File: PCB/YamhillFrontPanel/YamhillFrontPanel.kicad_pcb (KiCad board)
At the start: 2 copper layers, 110 x 50 mm, 6 parts

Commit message: Rev A Front Panel
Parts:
- added C1: 100n, Capacitor_SMD:C_0805_2012Metric, F.Cu at (75.5, 113.0)
- added C10: 100n, Capacitor_SMD:C_0805_2012Metric, F.Cu at (110.0, 136.3)
- added C11: 100n, Capacitor_SMD:C_0805_2012Metric, F.Cu at (113.8, 136.3)
- added C12: 100n, Capacitor_SMD:C_0805_2012Metric, F.Cu at (101.3, 130.4)
- added C13: 100n, Capacitor_SMD:C_0805_2012Metric, F.Cu at (177.6, 101.8)
- added C14: 10n, Capacitor_SMD:C_0805_2012Metric, F.Cu at (106.6, 134.0)
- added C15: 100n, Capacitor_SMD:C_0805_2012Metric, F.Cu at (117.7, 138.6)
- added C16: 100n, Capacitor_SMD:C_0805_2012Metric, F.Cu at (164.7, 110.8)
- added C17: 100n, Capacitor_SMD:C_0805_2012Metric, F.Cu at (78.9, 54.3)
- added C18: 100n, Capacitor_SMD:C_0805_2012Metric, F.Cu at (117.7, 142.1)
- added C19: 100n, Capacitor_SMD:C_0805_2012Metric, F.Cu at (207.0, 65.0)
- added C2: 100n, Capacitor_SMD:C_0805_2012Metric, F.Cu at (71.9, 92.4)
- added C20: 100n, Capacitor_SMD:C_0805_2012Metric, F.Cu at (106.5, 142.1)
- added C21: 100n, Capacitor_SMD:C_0805_2012Metric, F.Cu at (207.0, 77.0)
- added C22: 100n, Capacitor_SMD:C_0805_2012Metric, F.Cu at (207.0, 89.0)
- added C23: 100n, Capacitor_SMD:C_0805_2012Metric, F.Cu at (207.0, 101.0)
- added C24: 10u, Capacitor_SMD:CP_Elec_4x4.5, F.Cu at (139.2, 85.9)
- added C25: 10n, Capacitor_SMD:C_0805_2012Metric, F.Cu at (146.6, 95.0)
- added C26: 1u, Capacitor_SMD:C_0805_2012Metric, F.Cu at (143.1, 136.0)
- added C27: 100n, Capacitor_SMD:C_0805_2012Metric, F.Cu at (158.2, 110.8)
- added C28: 1u, Capacitor_SMD:C_0805_2012Metric, F.Cu at (128.7, 99.3)
- added C29: 1u, Capacitor_SMD:C_0805_2012Metric, F.Cu at (146.6, 98.4)
- added C3: 100n, Capacitor_SMD:C_0805_2012Metric, F.Cu at (75.8, 80.0)
- added C30: 2.7n, Capacitor_SMD:C_0805_2012Metric, F.Cu at (146.6, 102.1)
- added C31: 10u, Capacitor_SMD:CP_Elec_4x4.5, F.Cu at (124.0, 107.2)
- added C32: 10u, Capacitor_SMD:CP_Elec_4x4.5, F.Cu at (111.9, 86.0)
- added C33: 10u, Capacitor_SMD:CP_Elec_4x4.5, F.Cu at (116.6, 64.4)
- added C34: 100n, Capacitor_SMD:C_0805_2012Metric, F.Cu at (100.5, 96.8)
- added C35: 1u, Capacitor_SMD:C_0805_2012Metric, F.Cu at (104.5, 96.8)
- added C36: 1u, Capacitor_SMD:C_0805_2012Metric, F.Cu at (124.4, 81.5)
- added C37: 1u, Capacitor_SMD:C_0805_2012Metric, F.Cu at (108.1, 68.8)
- added C38: 1u, Capacitor_SMD:C_0805_2012Metric, F.Cu at (85.2, 96.9)
- added C39: 100n, Capacitor_SMD:C_0805_2012Metric, F.Cu at (100.5, 101.4)
- added C4: 100n, Capacitor_SMD:C_0805_2012Metric, F.Cu at (71.9, 59.4)
- added C40: 100u, Capacitor_SMD:CP_Elec_6.3x5.9, F.Cu at (115.0, 108.2)
- added C41: 1u, Capacitor_SMD:C_0805_2012Metric, F.Cu at (111.3, 100.5)
- added C42: 1u, Capacitor_SMD:C_0805_2012Metric, F.Cu at (98.4, 74.5)
- added C43: 1u, Capacitor_SMD:C_0805_2012Metric, F.Cu at (129.4, 76.3)
- added C44: 100n, Capacitor_SMD:C_0805_2012Metric, F.Cu at (152.9, 107.0)
- added C45: 100n, Capacitor_SMD:C_0805_2012Metric, F.Cu at (157.5, 107.0)
- added C5: 100n, Capacitor_SMD:C_0805_2012Metric, F.Cu at (90.0, 126.1)
- added C6: 100n, Capacitor_SMD:C_0805_2012Metric, F.Cu at (90.0, 117.0)
- added C7: 100n, Capacitor_SMD:C_0805_2012Metric, F.Cu at (68.6, 113.0)
- added C8: 100n, Capacitor_SMD:C_0805_2012Metric, F.Cu at (68.6, 80.0)
- added C9: 100n, Capacitor_SMD:C_0805_2012Metric, F.Cu at (167.4, 141.5)
- added D1: MBRX120LF-TP, Diode_SMD:D_SOD-123, F.Cu at (200.0, 146.5)
- added D2: WS2812B, LED_SMD:LED_WS2812B_PLCC4_5.0x5.0mm_P3.2mm, B.Cu at (163.2, 118.7)
- added D3: WS2812B, LED_SMD:LED_WS2812B_PLCC4_5.0x5.0mm_P3.2mm, B.Cu at (72.0, 55.0)
- added D4: LED, LED_SMD:LED_0805_2012Metric, B.Cu at (203.0, 65.0)
- added D5: LED, LED_SMD:LED_0805_2012Metric, B.Cu at (203.0, 77.0)
- added D6: LED, LED_SMD:LED_0805_2012Metric, B.Cu at (203.0, 89.0)
- added D7: LED, LED_SMD:LED_0805_2012Metric, B.Cu at (203.0, 101.0)
- added J1: +3.3V In, Connector_PinHeader_2.54mm:PinHeader_1x02_P2.54mm_Vertical, F.Cu at (182.0, 147.0)
- added J10: Ext. ADC, Connector_PinHeader_2.54mm:PinHeader_1x08_P2.54mm_Vertical, F.Cu at (154.6, 147.0)
- added J11: CLK2, EtherkitKicadLibrary:SMA_Jack_Vertical, F.Cu at (68.0, 136.0)
- added J12: Mute, Connector_PinHeader_2.54mm:PinHeader_1x08_P2.54mm_Vertical, F.Cu at (128.0, 147.0)
- added J13: CLK4, EtherkitKicadLibrary:SMA_Jack_Vertical, F.Cu at (81.0, 136.0)
- added J14: REF_IN, EtherkitKicadLibrary:SMA_Jack_Vertical, F.Cu at (94.0, 136.0)
- added J15: Mic Power Jumper, Connector_PinHeader_2.54mm:PinHeader_1x02_P2.54mm_Vertical, F.Cu at (138.0, 109.8)
- added J16: Microphone, Connector_RJ:RJ45_OST_PJ012-8P8CX_Vertical, B.Cu at (155.0, 120.0)
- added J17: Mic Output, Connector_PinHeader_2.54mm:PinHeader_1x02_P2.54mm_Vertical, F.Cu at (150.4, 137.9)
- added J18: AF In, Connector_PinHeader_2.54mm:PinHeader_1x02_P2.54mm_Vertical, F.Cu at (84.3, 104.2)
- added J19: AF Jumper, Connector_PinHeader_2.54mm:PinHeader_1x02_P2.54mm_Vertical, F.Cu at (123.4, 86.3)
- added J2: Paddles, EtherkitKicadLibrary:Kycon_STX-3680-5NB, B.Cu at (97.0, 122.0)
- added J20: Speaker, EtherkitKicadLibrary:Ole_Wolff_OWS-091630W50A-8, F.Cu at (70.0, 124.0)
- added J21: Headphones, EtherkitKicadLibrary:Kycon_STX-3680-5NB, B.Cu at (110.0, 122.0)
- added J22: I/Q In, Connector_PinHeader_2.54mm:PinHeader_1x03_P2.54mm_Vertical, F.Cu at (152.5, 102.7)
- added J3: +5V In, Connector_PinHeader_2.54mm:PinHeader_1x02_P2.54mm_Vertical, F.Cu at (192.0, 147.0)
- added J4: USB VBUS, Connector_PinHeader_2.54mm:PinHeader_1x02_P2.54mm_Vertical, F.Cu at (205.0, 147.0)
- added J5: UART, Connector_PinHeader_2.54mm:PinHeader_1x03_P2.54mm_Vertical, F.Cu at (217.2, 109.9)
- added J6: Transmit, Connector_PinHeader_2.54mm:PinHeader_1x10_P2.54mm_Vertical, F.Cu at (95.0, 147.0)
- added J7: GPIO, Connector_PinHeader_2.54mm:PinHeader_1x12_P2.54mm_Vertical, F.Cu at (154.2, 91.9)
- added J8: CLK0, EtherkitKicadLibrary:SMA_Jack_Vertical, F.Cu at (55.0, 136.0)
- added J9: Osc Outputs, Connector_PinHeader_2.54mm:PinHeader_1x04_P2.54mm_Vertical, F.Cu at (78.5, 147.0)
- added L1: Fair-Rite 2512066017Y1, Inductor_SMD:L_1206_3216Metric, F.Cu at (146.2, 140.1)
- added Q1: 2N7002, Package_TO_SOT_SMD:SOT-23, F.Cu at (124.5, 75.5)
- added Q2: 2N7002, Package_TO_SOT_SMD:SOT-23, F.Cu at (103.4, 73.8)
- added Q3: 2N7002, Package_TO_SOT_SMD:SOT-23, F.Cu at (123.2, 134.4)
- added Q4: 2N7002, Package_TO_SOT_SMD:SOT-23, F.Cu at (118.2, 125.6)
- added R1: 47k, Resistor_SMD:R_0805_2012Metric, F.Cu at (161.0, 130.0)
- added R10: 47, Resistor_SMD:R_0805_2012Metric, F.Cu at (121.8, 138.6)
- added R11: 47, Resistor_SMD:R_0805_2012Metric, F.Cu at (121.8, 142.1)
- added R12: 10k, Resistor_SMD:R_0805_2012Metric, F.Cu at (177.6, 98.4)
- added R13: 10k, Resistor_SMD:R_0805_2012Metric, F.Cu at (102.6, 142.1)
- added R14: 10k, Resistor_SMD:R_0805_2012Metric, F.Cu at (177.6, 105.3)
- added R15: 470, Resistor_SMD:R_0805_2012Metric, F.Cu at (176.5, 143.4)
- added R16: 47, Resistor_SMD:R_0805_2012Metric, F.Cu at (106.5, 138.5)
- added R17: 4.7k, Resistor_SMD:R_0805_2012Metric, F.Cu at (127.6, 136.9)
- added R18: 4.7k, Resistor_SMD:R_0805_2012Metric, F.Cu at (127.5, 140.3)
- added R19: 330, Resistor_SMD:R_0805_2012Metric, F.Cu at (203.0, 65.0)
- added R2: 47k, Resistor_SMD:R_0805_2012Metric, F.Cu at (161.0, 125.0)
- added R20: 330, Resistor_SMD:R_0805_2012Metric, F.Cu at (203.0, 77.0)
- added R21: 330, Resistor_SMD:R_0805_2012Metric, F.Cu at (203.0, 89.0)
- added R22: 330, Resistor_SMD:R_0805_2012Metric, F.Cu at (203.0, 101.0)
- added R23: 7.5k, Resistor_SMD:R_0805_2012Metric, F.Cu at (131.3, 109.8)
- added R24: 47, Resistor_SMD:R_0805_2012Metric, F.Cu at (145.3, 90.3)
- added R25: 470, Resistor_SMD:R_0805_2012Metric, F.Cu at (136.0, 104.7)
- added R26: 5k trim, EtherkitKicadLibrary:Bournes_PTV09A, F.Cu at (136.0, 132.0)
- added R27: 10k, Resistor_SMD:R_0805_2012Metric, F.Cu at (133.3, 88.2)
- added R28: 10k, Resistor_SMD:R_0805_2012Metric, F.Cu at (140.8, 102.1)
- added R29: 100k, Resistor_SMD:R_0805_2012Metric, F.Cu at (132.4, 99.3)
- added R3: 47k, Resistor_SMD:R_0805_2012Metric, F.Cu at (161.0, 135.0)
- added R30: 10k, Resistor_SMD:R_0805_2012Metric, F.Cu at (128.7, 104.7)
- added R31: 470, Resistor_SMD:R_0805_2012Metric, F.Cu at (128.7, 93.6)
- added R32: 270k, Resistor_SMD:R_0805_2012Metric, F.Cu at (132.4, 93.6)
- added R33: 10k, Resistor_SMD:R_0805_2012Metric, F.Cu at (132.4, 104.7)
- added R34: 10k, Resistor_SMD:R_0805_2012Metric, F.Cu at (106.5, 86.1)
- added R35: 47, Resistor_SMD:R_0805_2012Metric, F.Cu at (117.5, 70.4)
- added R36: 100k, Resistor_SMD:R_0805_2012Metric, F.Cu at (107.8, 79.8)
- added R37: 100k, Resistor_SMD:R_0805_2012Metric, F.Cu at (120.4, 80.6)
- added R38: 10k, Resistor_SMD:R_0805_2012Metric, F.Cu at (117.2, 86.1)
- added R39: 47, Resistor_SMD:R_0805_2012Metric, F.Cu at (104.5, 92.8)
- added R4: 47, Resistor_SMD:R_0805_2012Metric, F.Cu at (109.9, 132.9)
- added R40: 1k, Resistor_SMD:R_0805_2012Metric, F.Cu at (112.0, 68.8)
- added R41: 100, Resistor_SMD:R_0805_2012Metric, F.Cu at (85.2, 92.0)
- added R42: 10k, EtherkitKicadLibrary:Alps_RK09L1140, B.Cu at (126.0, 122.0)
- added R43: 10k, Resistor_SMD:R_0805_2012Metric, F.Cu at (120.4, 75.5)
- added R44: 150, Resistor_SMD:R_0805_2012Metric, F.Cu at (117.9, 117.9)
- added R45: 100k, Resistor_SMD:R_0805_2012Metric, F.Cu at (104.9, 107.4)
- added R46: 1k, Resistor_SMD:R_0805_2012Metric, F.Cu at (107.8, 74.4)
- added R47: 100k, Resistor_SMD:R_0805_2012Metric, F.Cu at (100.5, 105.1)
- added R48: 470, Resistor_SMD:R_0805_2012Metric, F.Cu at (103.4, 68.8)
- added R49: 1k, Resistor_SMD:R_0805_2012Metric, F.Cu at (124.5, 70.0)
- added R5: 47, Resistor_SMD:R_0805_2012Metric, F.Cu at (113.8, 132.9)
- added R50: 100k, Resistor_SMD:R_0805_2012Metric, F.Cu at (98.4, 70.6)
- added R51: 100k, Resistor_SMD:R_0805_2012Metric, F.Cu at (129.4, 72.4)
- added R52: 4.7k, Resistor_SMD:R_0805_2012Metric, F.Cu at (118.2, 130.8)
- added R53: 4.7k, Resistor_SMD:R_0805_2012Metric, F.Cu at (118.2, 134.3)
- added R6: 47k, Resistor_SMD:R_0805_2012Metric, F.Cu at (164.0, 130.0)
- added R7: 47k, Resistor_SMD:R_0805_2012Metric, F.Cu at (164.0, 125.0)
- added R8: 47k, Resistor_SMD:R_0805_2012Metric, F.Cu at (164.0, 135.0)
- added R9: 47, Resistor_SMD:R_0805_2012Metric, F.Cu at (101.6, 138.7)
- added S1: PUSHBUTTON_TACTILE, EtherkitKicadLibrary:E-Switch_TL1105, B.Cu at (212.0, 65.0)
- added S2: PUSHBUTTON_TACTILE, EtherkitKicadLibrary:E-Switch_TL1105, B.Cu at (212.0, 77.0)
- added S3: PUSHBUTTON_TACTILE, EtherkitKicadLibrary:E-Switch_TL1105, B.Cu at (212.0, 89.0)
- added S4: PUSHBUTTON_TACTILE, EtherkitKicadLibrary:E-Switch_TL1105, B.Cu at (212.0, 101.0)
- added SW1: Tune, EtherkitKicadLibrary:Bournes_PEC11R-4xxxF-Sxxxx, B.Cu at (72.0, 101.0)
- added SW2: Multifunction, EtherkitKicadLibrary:Bournes_PEC11R-4xxxF-Sxxxx, B.Cu at (72.0, 68.0)
- added U1: 4" TFT LCD ST7796S, EtherkitKicadLibrary:ST7796_4.0in, B.Cu at (146.4, 83.0)
- added U2: ADS1115IDGS, Package_SO:TSSOP-10_3x3mm_P0.5mm, F.Cu at (162.2, 141.3)
- added U3: Pico, MCU_RaspberryPi_and_Boards:RPi_Pico_SMD_TH, F.Cu at (194.0, 126.7)
- added U4: ATX-H11-F-25.000MHZ-F25-T, EtherkitKicadLibrary:ASTX-H11-25.000MHZ-T, F.Cu at (101.4, 134.6)
- added U5: Si5351C, Package_DFN_QFN:VQFN-20-1EP_3x3mm_P0.45mm_EP1.55x1.55mm_ThermalVias, F.Cu at (112.0, 140.9)
- added U6: TCAL6416, Package_SO:TSSOP-24_6.1x7.8mm_P0.65mm, F.Cu at (188.1, 104.2)
- added U7: TLV9362, Package_SO:SOIC-8_3.9x4.9mm_P1.27mm, F.Cu at (139.3, 95.6)
- added U8: TLV9362, Package_SO:SOIC-8_3.9x4.9mm_P1.27mm, F.Cu at (114.1, 75.5)
- added U9: LM4875, Package_SO:TSSOP-8_3x3mm_P0.65mm, F.Cu at (106.0, 101.8)
- G***, Ref**: moved to F.Cu
- moved Ref** 119.5 mm to (90.1, 54.9), turned to 0 degrees
- moved G*** 105.7 mm to (206.0, 57.4), turned to 0 degrees
- moved H3 70.7 mm to (55.0, 145.0)
- moved H4 51.0 mm to (215.0, 145.0)
- moved H1 50.0 mm to (55.0, 55.0)
- moved H2 10.0 mm to (215.0, 55.0)
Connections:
- H1 pad 1: unconnected-(H1-Pad1) -> GNDD
- H2 pad 1: unconnected-(H2-Pad1) -> GNDD
- H3 pad 1: unconnected-(H3-Pad1) -> GNDD
- H4 pad 1: unconnected-(H4-Pad1) -> GNDD
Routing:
- net +5V: track 0.00 -> 431.4 mm, vias 0 -> 10
- net ENC1_A: track 0.00 -> 295.7 mm
- net ENC1_B: track 0.00 -> 289.8 mm, vias 0 -> 1
- net +3.3V: track 0.00 -> 284.7 mm, vias 0 -> 12
- net ENC2_B: track 0.00 -> 241.1 mm, vias 0 -> 2
- net ENC2_A: track 0.00 -> 237.8 mm, vias 0 -> 2
- net MUTE: track 0.00 -> 195.0 mm, vias 0 -> 5
- net ENC1_SW: track 0.00 -> 189.1 mm, vias 0 -> 1
- net SDA_3V3: track 0.00 -> 167.0 mm, vias 0 -> 3
- net SCL_3V3: track 0.00 -> 162.5 mm, vias 0 -> 3
- net ENC2_SW: track 0.00 -> 158.1 mm, vias 0 -> 2
- net Net-(D2-DOUT): track 0.00 -> 156.8 mm, vias 0 -> 2
- net SPI_TX: track 0.00 -> 149.7 mm
- net MCU_DAC: track 0.00 -> 141.5 mm, vias 0 -> 6
- net PDL_B: track 0.00 -> 134.0 mm, vias 0 -> 1
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- added copper zone on F.Cu, net GND
- added copper zone on B.Cu, net GNDD
- added copper zone on F.Cu, net GNDD
- removed copper zone on B.Cu, net (none)
- removed copper zone on F.Cu, net (none)
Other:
- board size 110 x 50 mm -> 170 x 100 mm
- board text added: "+3.3V"
- board text added: "+5V"
- board text added: "AF"
- board text added: "AIN0"
- board text added: "AIN1"
- board text added: "AIN2"
- board text added: "AIN3"
- board text added: "CLK0"
- board text added: "CLK1"
- board text added: "CLK2"
- board text added: "CLK3"
- board text added: "CLK4"
- board text added: "Front Panel Etherkit 2023"
- board text added: "GND"
- board text added: "I"
- board text added: "MIC GAIN"
- board text added: "Mic"
- board text added: "Mute"
- board text added: "P06"
- board text added: "P07"
- board text added: "P10"
- board text added: "P11"
- board text added: "P12"
- board text added: "P13"
- board text added: "Q"
- board text added: "REF IN"
- board text added: "RX"
- board text added: "TX"
- board text removed: "Sample Board Etherkit 2023"

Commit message: Update all PCBs for first tranche order
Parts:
- J20: footprint EtherkitKicadLibrary:Ole_Wolff_OWS-091630W50A-8 -> EtherkitKicadLibrary:CUI_CMS-160916-30-3; moved to B.Cu
- R26: footprint EtherkitKicadLibrary:Bournes_PTV09A -> EtherkitKicadLibrary:Bournes_PTV09A-4
- moved J20 2.57 mm to (72.5, 123.4), turned to 180 degrees
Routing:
- net +3.3V: track 284.7 -> 64.0 mm, vias 12 -> 10
- net GNDD: track 0.00 -> 91.0 mm, vias 4 -> 31
- net GND: track 0.00 -> 56.5 mm
- net Net-(J20-Pin_2): track 43.0 -> 59.4 mm, vias 0 -> 1
- net Net-(J20-Pin_1): track 48.7 -> 60.4 mm, vias 0 -> 1
- net Net-(C26-Pad2): track 11.7 -> 5.61 mm
- net PDL_A: track 126.1 -> 129.1 mm
- net Net-(U5-VDDOB): track 11.9 -> 14.7 mm
- net Net-(J14-In): track 23.0 -> 20.3 mm
- net +5V: track 431.4 -> 433.0 mm
- net PDL_B: track 134.0 -> 135.4 mm
- net Net-(D2-DOUT): track 156.8 -> 158.1 mm
- net CLK3: track 32.7 -> 33.9 mm
- net CLK2: track 52.5 -> 53.5 mm
- net MIC_SAMPLE: track 120.0 -> 119.0 mm
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- added copper zone on In2.Cu, net +3.3V
- added copper zone on In1.Cu, net GNDD
- removed copper zone on B.Cu, net GNDD
- removed copper zone on F.Cu, net GNDD
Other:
- copper layers 2 -> 4
- board text added: "Front Panel Etherkit 2024"
- board text removed: "Front Panel Etherkit 2023"

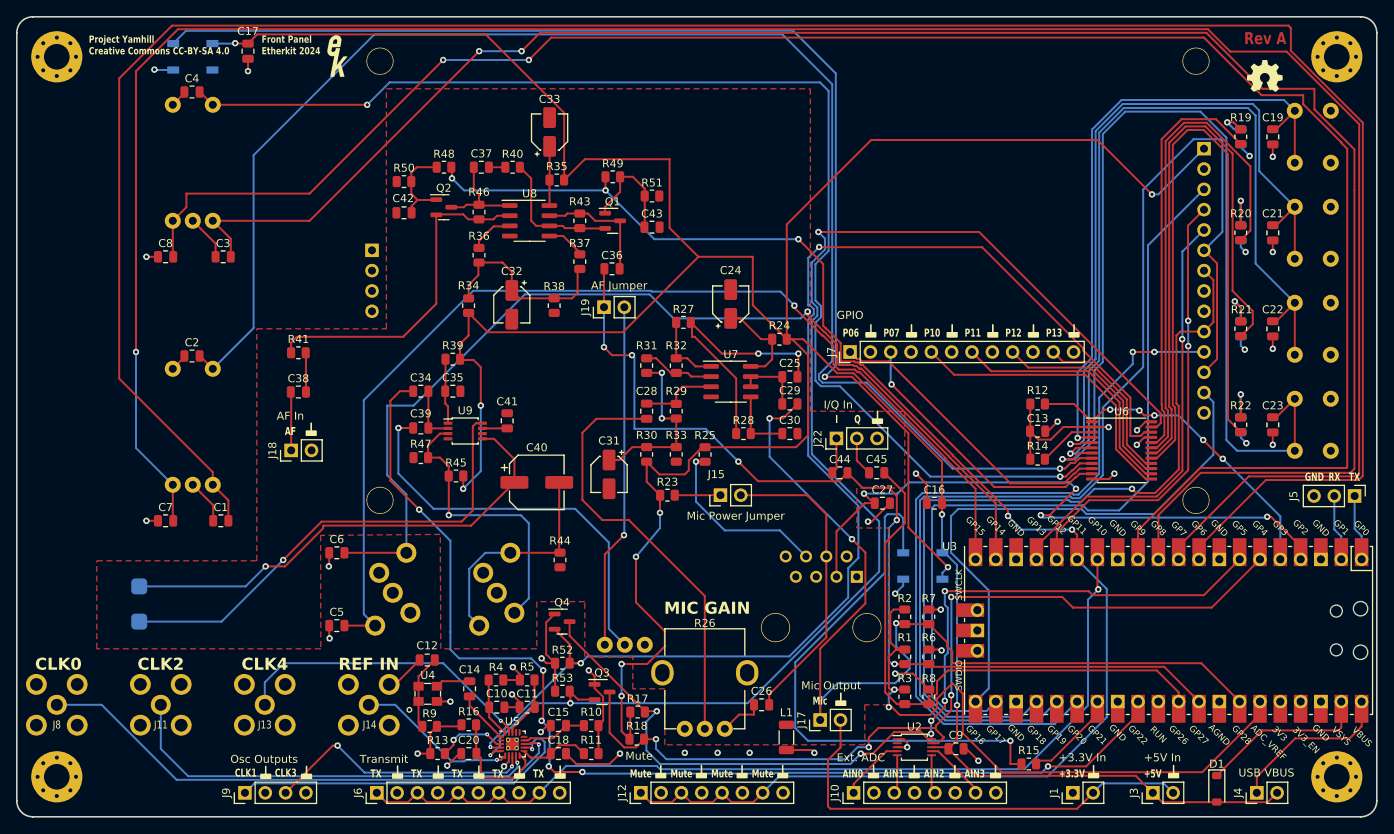
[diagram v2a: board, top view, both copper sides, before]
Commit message: Arch document update
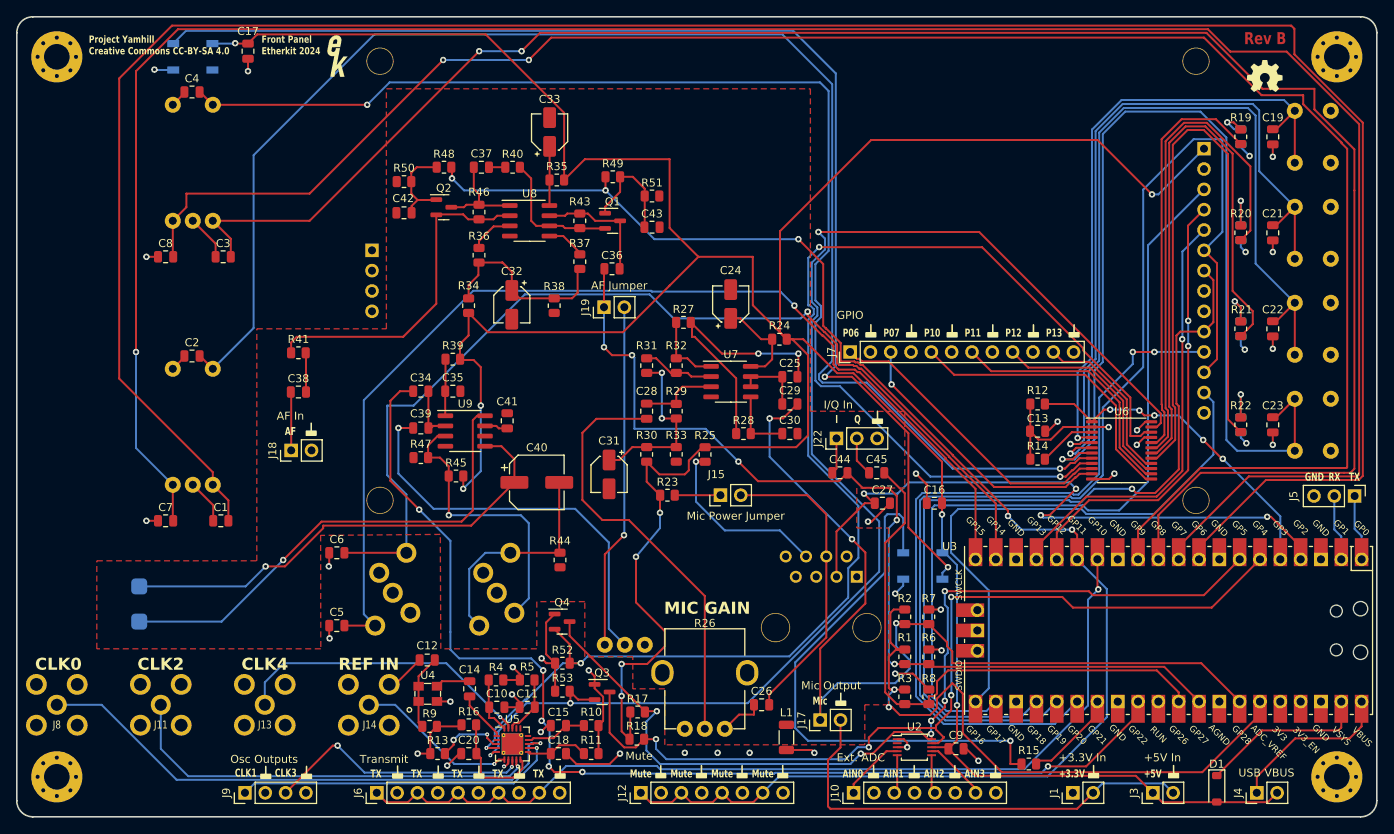
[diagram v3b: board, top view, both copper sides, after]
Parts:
- U5: footprint Package_DFN_QFN:VQFN-20-1EP_3x3mm_P0.45mm_EP1.55x1.55mm_ThermalVias -> Package_DFN_QFN:QFN-20-1EP_4x4mm_P0.5mm_EP2.7x2.7mm_ThermalVias
- U6: value TCAL6416 -> TCAL6416PWR
- U9: footprint Package_SO:TSSOP-8_3x3mm_P0.65mm -> Package_SO:SOIC-8_3.9x4.9mm_P1.27mm
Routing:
- net CLK1: track 45.0 -> 41.1 mm
- net Net-(J20-Pin_2): track 59.4 -> 60.5 mm
- net Net-(U9-VDD): track 8.16 -> 7.10 mm
- net Net-(U5-VDDOA): track 8.90 -> 7.94 mm
- net SCL_3V3: track 163.2 -> 164.1 mm
- net Net-(U5-VDDOB): track 14.7 -> 13.8 mm
- net Net-(J20-Pin_1): track 60.4 -> 59.7 mm
- net +5V: track 433.0 -> 433.7 mm
- net CLK0: track 68.6 -> 69.1 mm
- net Net-(U5-VDDOD): track 8.25 -> 7.73 mm
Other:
- board text added: "Rev B"
- board text removed: "Rev A"

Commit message: Front Panel Rev B revisions
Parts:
- removed the C37 at (108.1, 68.8)
- removed the J10 at (154.6, 147.0)
- removed the J9 at (78.5, 147.0)
- removed the R36 at (107.8, 79.8)
- removed the R39 at (104.5, 92.8)
- added C11: 100n, Capacitor_SMD:C_0805_2012Metric, F.Cu at (166.7, 96.8)
- added C22: 1u, Capacitor_SMD:C_0805_2012Metric, F.Cu at (54.4, 125.4)
- added C23: 1u, Capacitor_SMD:C_0805_2012Metric, F.Cu at (66.2, 125.4)
- added C25: 100n, Capacitor_SMD:C_0805_2012Metric, F.Cu at (58.9, 125.4)
- added C26: 100n, Capacitor_SMD:C_0805_2012Metric, F.Cu at (70.7, 125.4)
- added C32: 1u, Capacitor_SMD:C_0805_2012Metric, F.Cu at (98.0, 103.1)
- added C34: 10u, Capacitor_SMD:CP_Elec_4x4.5, F.Cu at (105.8, 95.0)
- added C36: 1n, Capacitor_SMD:C_0805_2012Metric, F.Cu at (90.2, 93.6)
- added C38: 1u, Capacitor_SMD:C_0805_2012Metric, F.Cu at (108.8, 79.6)
- added C43: 1n, Capacitor_SMD:C_0805_2012Metric, F.Cu at (106.0, 74.4)
- added C44: 1u, Capacitor_SMD:C_0805_2012Metric, F.Cu at (116.4, 81.1)
- added C45: 1n, Capacitor_SMD:C_0805_2012Metric, F.Cu at (119.3, 75.4)
- added C50: 1u, Capacitor_SMD:C_0805_2012Metric, F.Cu at (128.5, 81.5)
- added C51: 1u, Capacitor_SMD:C_0805_2012Metric, F.Cu at (131.1, 68.9)
- added C53: 10u, Capacitor_SMD:CP_Elec_4x4.5, F.Cu at (145.1, 62.3)
- added C57: 1u, Capacitor_SMD:C_0805_2012Metric, F.Cu at (139.3, 75.5)
- added C58: 1u, Capacitor_SMD:C_0805_2012Metric, F.Cu at (143.6, 70.4)
- added C61: 10u, Capacitor_SMD:CP_Elec_4x4.5, F.Cu at (106.6, 103.9)
- added C62: 1u, Capacitor_SMD:C_0805_2012Metric, F.Cu at (147.3, 73.0)
- added D8: MBRX120LF-TP, Diode_SMD:D_SOD-123, F.Cu at (134.7, 80.6)
- added D9: MBRX120LF-TP, Diode_SMD:D_SOD-123, F.Cu at (144.1, 80.6)
- added J11: P06, Connector_PinHeader_2.54mm:PinHeader_1x02_P2.54mm_Vertical, F.Cu at (154.2, 91.8)
- added J13: P10, Connector_PinHeader_2.54mm:PinHeader_1x02_P2.54mm_Vertical, F.Cu at (166.8, 91.8)
- added J14: P11, Connector_PinHeader_2.54mm:PinHeader_1x02_P2.54mm_Vertical, F.Cu at (173.1, 91.8)
- added J15: P12, Connector_PinHeader_2.54mm:PinHeader_1x02_P2.54mm_Vertical, F.Cu at (179.4, 91.8)
- added J16: P13, Connector_PinHeader_2.54mm:PinHeader_1x02_P2.54mm_Vertical, F.Cu at (185.7, 91.8)
- added J18: DAC Out, Connector_PinHeader_2.54mm:PinHeader_1x02_P2.54mm_Vertical, F.Cu at (170.0, 102.7)
- added J2: TX, Connector_PinHeader_2.54mm:PinHeader_1x02_P2.54mm_Vertical, F.Cu at (102.8, 147.0)
- added J20: +12V IN, Connector_PinHeader_2.54mm:PinHeader_1x02_P2.54mm_Vertical, F.Cu at (64.2, 147.0)
- added J21: AIN0, Connector_PinHeader_2.54mm:PinHeader_1x02_P2.54mm_Vertical, F.Cu at (153.5, 147.0)
- added J22: AIN1, Connector_PinHeader_2.54mm:PinHeader_1x02_P2.54mm_Vertical, F.Cu at (159.8, 147.0)
- added J23: AIN2, Connector_PinHeader_2.54mm:PinHeader_1x02_P2.54mm_Vertical, F.Cu at (166.1, 147.0)
- added J25: CLK1, Connector_PinHeader_2.54mm:PinHeader_1x02_P2.54mm_Vertical, F.Cu at (77.4, 147.0)
- added J26: CLK3, Connector_PinHeader_2.54mm:PinHeader_1x02_P2.54mm_Vertical, F.Cu at (83.6, 147.0)
- added J31: +5VA In, Connector_PinHeader_2.54mm:PinHeader_1x02_P2.54mm_Vertical, F.Cu at (82.7, 125.8)
- added J37: AF Det Out, Connector_PinHeader_2.54mm:PinHeader_1x02_P2.54mm_Vertical, F.Cu at (102.1, 110.5)
- added J4: TX, Connector_PinHeader_2.54mm:PinHeader_1x02_P2.54mm_Vertical, F.Cu at (115.3, 147.0)
- added J5: MUTE, Connector_PinHeader_2.54mm:PinHeader_1x02_P2.54mm_Vertical, F.Cu at (143.9, 147.0)
- added J8: MUTE, Connector_PinHeader_2.54mm:PinHeader_1x02_P2.54mm_Vertical, F.Cu at (125.0, 147.0)
- added R25: 100, Resistor_SMD:R_0805_2012Metric, F.Cu at (82.4, 90.0)
- added R26: 100k, Resistor_SMD:R_0805_2012Metric, F.Cu at (94.4, 103.1)
- added R29: 47, Resistor_SMD:R_0805_2012Metric, F.Cu at (102.5, 90.8)
- added R30: 1k, Resistor_SMD:R_0805_2012Metric, F.Cu at (90.2, 90.0)
- added R35: 100k, Resistor_SMD:R_0805_2012Metric, F.Cu at (104.9, 78.8)
- added R53: 100k, Resistor_SMD:R_0805_2012Metric, F.Cu at (135.3, 72.1)
- added R54: 4.7k, Resistor_SMD:R_0805_2012Metric, F.Cu at (128.3, 75.5)
- added R55: 100k, Resistor_SMD:R_0805_2012Metric, F.Cu at (128.3, 65.2)
- added R56: 47, Resistor_SMD:R_0805_2012Metric, F.Cu at (139.6, 60.9)
- added R58: 100k, Resistor_SMD:R_0805_2012Metric, F.Cu at (139.3, 72.1)
- added R59: 10k, Resistor_SMD:R_0805_2012Metric, F.Cu at (132.6, 62.4)
- added R60: 1k, Resistor_SMD:R_0805_2012Metric, F.Cu at (139.3, 79.0)
- added R61: 10k, Resistor_SMD:R_0805_2012Metric, F.Cu at (147.3, 68.0)
- added R64: 100k, Resistor_SMD:R_0805_2012Metric, F.Cu at (101.4, 104.1)
- added R66: 1k, Resistor_SMD:R_0805_2012Metric, F.Cu at (143.5, 75.6)
- added TP1: GNDA, TestPoint:TestPoint_THTPad_D2.0mm_Drill1.0mm, F.Cu at (150.0, 112.0)
- added TP2: GNDD, TestPoint:TestPoint_THTPad_D2.0mm_Drill1.0mm, F.Cu at (187.1, 147.0)
- added U10: TLV9362, Package_SO:SOIC-8_3.9x4.9mm_P1.27mm, F.Cu at (98.0, 97.0)
- added U13: TLV9362, Package_SO:SOIC-8_3.9x4.9mm_P1.27mm, F.Cu at (137.4, 66.5)
- added U2: MCP4725A1T-E/CH, Package_TO_SOT_SMD:SOT-23-6, F.Cu at (171.2, 96.8)
- added U6: UA78M33CKVURG3, Package_TO_SOT_SMD:TO-252-2, F.Cu at (57.6, 116.5)
- added U7: UA78M05IKVURG3, Package_TO_SOT_SMD:TO-252-2, F.Cu at (69.4, 116.5)
- J1: value +3.3V In -> TX
- J12: value Mute -> P07; footprint Connector_PinHeader_2.54mm:PinHeader_1x08_P2.54mm_Vertical -> Connector_PinHeader_2.54mm:PinHeader_1x02_P2.54mm_Vertical
- J3: value +5V In -> TX
- J34: renamed from J19; footprint Connector_PinHeader_2.54mm:PinHeader_1x02_P2.54mm_Vertical -> Connector_PinHeader_2.54mm:PinHeader_2x02_P2.54mm_Vertical
- J36: renamed from J20; footprint EtherkitKicadLibrary:CUI_CMS-160916-30-3 -> Connector_PinHeader_2.54mm:PinHeader_1x02_P2.54mm_Vertical; moved to F.Cu
- J6: value Transmit -> MUTE; footprint Connector_PinHeader_2.54mm:PinHeader_1x10_P2.54mm_Vertical -> Connector_PinHeader_2.54mm:PinHeader_1x02_P2.54mm_Vertical
- J7: value GPIO -> MUTE; footprint Connector_PinHeader_2.54mm:PinHeader_1x12_P2.54mm_Vertical -> Connector_PinHeader_2.54mm:PinHeader_1x02_P2.54mm_Vertical
- L1: footprint Inductor_SMD:L_1206_3216Metric -> Inductor_SMD:L_1206_3216Metric_Pad1.42x1.75mm_HandSolder
- R34: renamed from R41; value 100 -> 1k
- R40: renamed from R46; value 1k -> 10k
- moved J1 85.5 mm to (96.5, 147.0)
- moved J3 82.9 mm to (109.1, 147.0)
- moved J12 64.1 mm to (160.5, 91.8)
- moved J7 59.6 mm to (131.3, 147.0)
- moved J6 42.6 mm to (137.6, 147.0)
- moved R34 17.6 mm to (100.3, 82.9), turned to 90 degrees
- moved C46 14.3 mm to (124.5, 62.9), turned to 180 degrees
- moved J36 13.1 mm to (82.7, 115.2), turned to 90 degrees
- moved C59 11.5 mm to (122.3, 97.0)
- moved U14 11.5 mm to (117.0, 98.3)
- moved C55 11.5 mm to (111.5, 97.9)
- moved R63 11.5 mm to (115.9, 103.9)
- moved C56 11.5 mm to (111.5, 93.3)
- moved C60 11.5 mm to (115.5, 93.3)
- moved R62 11.5 mm to (111.5, 101.6)
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- renumbered C5 to C1, C7 to C10, C13 to C12, C2 to C13, C16 to C14, C3 to C15, C8 to C16, C4 to C18, C12 to C19, C21 to C2, C14 to C20, C9 to C21, C10 to C24, C11 to C27, C20 to C28, C15 to C29, C22 to C3, C18 to C30, C38 to C31, C27 to C33, C26 to C35, C28 to C37, C31 to C39, C23 to C4, C42 to C40, C33 to C41, C24 to C42, C43 to C46, C32 to C47, C36 to C48, C30 to C49, C19 to C5, C25 to C52, C29 to C54, C39 to C55, C34 to C56, C41 to C59, C35 to C60, C40 to C63, C1 to C7, C44 to C8, C45 to C9, D4 to D1, D5 to D3, D6 to D4, D3 to D5, D7 to D6, D1 to D7, H3 to H2, H2 to H3, J22 to J10, J5 to J17, J4 to J19, J14 to J24, J8 to J27, J11 to J28, J13 to J29, J18 to J30, J16 to J32, J15 to J33, J17 to J35, J21 to J38, J2 to J9, Q4 to Q1, Q3 to Q2, Q2 to Q3, Q1 to Q4, R14 to R1, R19 to R10, R20 to R11, R21 to R12, R22 to R13, R17 to R14, R18 to R15, R9 to R16, R52 to R17, R13 to R18, R53 to R19, R4 to R20, R5 to R21, R16 to R22, R10 to R23, R11 to R24, R25 to R27, R23 to R28, R7 to R3, R26 to R31, R30 to R32, R29 to R36, R31 to R37, R35 to R38, R50 to R39, R1 to R4, R24 to R41, R48 to R42, R32 to R43, R34 to R44, R40 to R45, R37 to R46, R49 to R47, R27 to R48, R38 to R49, R6 to R5, R51 to R50, R43 to R51, R28 to R52, R42 to R57, R12 to R6, R47 to R62, R45 to R63, R44 to R65, R3 to R7, R15 to R9, U6 to U1, U8 to U11, U7 to U12, U9 to U14, U2 to U5, U5 to U8, U1 to U9
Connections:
- C31 pad 2: Net-(C38-Pad2) -> Net-(C31-Pad2)
- C35 pad 1: Net-(J15-Pin_2) -> Net-(J33-Pin_2)
- C47 pad 1: Net-(C32-Pad1) -> V_GND
- C60 pad 2: Net-(U9-VDD) -> +5VA
- J1 pad 1: +3.3V -> TX
- J1 pad 2: GND -> GNDD
- J12 pad 1: MUTE -> P07
- J3 pad 1: +5V -> TX
- J3 pad 2: GND -> GNDD
- J32 pad 2: GNDD -> unconnected-(J32-Pad2)
- J32 pad 3: PTT -> Net-(J32-Pad3)
- J32 pad 4: Net-(J15-Pin_2) -> GND
- J32 pad 5: GND -> Net-(J33-Pin_2)
- J32 pad 6: Net-(J16-Pad6) -> PTT
- J32 pad 7: unconnected-(J16-Pad7) -> GNDD
- J33 pad 2: Net-(J15-Pin_2) -> Net-(J33-Pin_2)
- J38 pad SN: Net-(U9-HPSENSE) -> Net-(J38-PadSN)
- J6 pad 1: TX -> MUTE
- J7 pad 1: P06 -> MUTE
- L1 pad 1: GNDD -> GND
- L1 pad 2: GND -> GNDD
- Q3 pad 3: Net-(Q2-D) -> Net-(Q3-D)
- R27 pad 1: Net-(J16-Pad6) -> Net-(J32-Pad3)
- R27 pad 2: +5V -> +5VA
- R28 pad 1: +5V -> +5VA
- R32 pad 1: +5V -> +5VA
- R34 pad 1: Net-(C38-Pad2) -> Net-(C36-Pad1)
- R38 pad 1: +5V -> +5VA
- R40 pad 2: Net-(Q2-D) -> Net-(Q3-D)
- R41 pad 1: +5V -> +5VA
- R44 pad 1: +5V -> +5VA
- R44 pad 2: Net-(C32-Pad1) -> V_GND
- R45 pad 1: Net-(C37-Pad1) (its old number) -> Net-(Q3-D)
- R46 pad 1: Net-(C32-Pad1) -> V_GND
- R49 pad 1: Net-(C32-Pad1) -> V_GND
- R62 pad 1: Net-(U9-HPSENSE) -> Net-(U14-HPSENSE)
- R62 pad 2: GND -> Net-(J38-PadSN)
- R63 pad 1: Net-(U9-HPSENSE) -> Net-(J38-PadSN)
- R63 pad 2: +5V -> +5VA
- U11 pad 1: Net-(Q2-D) -> Net-(Q3-D)
- U11 pad 3: V_GND -> Net-(U11A-+)
- U14 pad 1: Net-(U9-VDD) -> +5VA
- U14 pad 3: Net-(U9-HPSENSE) -> Net-(U14-HPSENSE)
- U14 pad 4: unconnected-(U9-DC_VOL-Pad4) -> +5VA
- U5 pad 7: Net-(J10-Pin_7) -> AF_DET
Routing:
- net +3.3V: track 64.0 -> 344.5 mm, vias 10 -> 21
- net +5VA: track 0.00 -> 199.4 mm, vias 0 -> 4
- net AF_DET: track 0.00 -> 141.4 mm, vias 0 -> 3
- net V_GND: track 5.50 -> 78.0 mm, vias 0 -> 2
- net Net-(D8-K): track 0.00 -> 60.8 mm, vias 0 -> 2
- net GND: track 56.5 -> 0.00 mm
- net Net-(J20-Pin_1): track 0.00 -> 41.5 mm
- net Net-(J15-Pin_2): track 38.4 -> 0.00 mm
- net Net-(U9-HPSENSE): track 35.7 -> 0.00 mm, vias 1 -> 0
- net Net-(C57-Pad2): track 0.00 -> 35.7 mm, vias 0 -> 2
- net SCL: track 119.0 -> 153.7 mm, vias 6 -> 8
- net SDA: track 113.7 -> 147.2 mm, vias 4 -> 7
- net Net-(J38-PadSN): track 0.00 -> 32.7 mm, vias 0 -> 1
- net Net-(J33-Pin_2): track 0.00 -> 32.7 mm
- net Net-(J32-Pad3): track 0.00 -> 27.9 mm, vias 0 -> 1
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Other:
- board text added: "GPIO"
- board text removed: "+3.3V"
- board text removed: "AIN3"

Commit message: Second tranche of PCBs
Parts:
- removed G***: LOGO, EtherkitKicadLibrary:OSHWLogo4mm
- removed Ref**: Val**, EtherkitKicadLibrary:EtherkitLogoSmall
- added C64: 100n, Capacitor_SMD:C_0805_2012Metric, F.Cu at (172.1, 96.8)
- added C65: 100n, Capacitor_SMD:C_0805_2012Metric, F.Cu at (167.1, 100.9)
- added C66: 100n, Capacitor_SMD:C_0805_2012Metric, F.Cu at (173.5, 106.6)
- added U15: MCP4725A1T-E/CH, Package_TO_SOT_SMD:SOT-23-6, F.Cu at (175.4, 96.8)
- J18: value DAC Out -> I/Q Out; footprint Connector_PinHeader_2.54mm:PinHeader_1x02_P2.54mm_Vertical -> Connector_PinHeader_2.54mm:PinHeader_1x03_P2.54mm_Vertical
- moved R6 4.52 mm to (181.9, 97.0)
- moved U2 3.34 mm to (167.9, 96.8)
- moved C12 2.28 mm to (179.4, 100.4)
- moved R1 2.28 mm to (179.4, 103.9)
- moved C11 2.10 mm to (164.6, 96.8)
- moved J18 0.76 mm to (170.8, 102.7)
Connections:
- C48 pad 1: I_SAMPLE -> Net-(J34-Pin_1)
- C50 pad 2: I_SAMPLE -> Net-(J34-Pin_1)
- J18 pad 2: GNDD -> Net-(J18-Pin_2)
- J34 pad 1: I_SAMPLE -> Net-(J34-Pin_1)
- U2 pad 1: Net-(J18-Pin_1) -> Net-(U2-VOUT)
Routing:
- net I_SAMPLE: track 133.5 -> 86.8 mm
- net +5V: track 435.0 -> 455.6 mm, vias 7 -> 9
- net Net-(U15-VOUT): track 0.00 -> 18.9 mm
- net Net-(J34-Pin_1): track 0.00 -> 11.7 mm
- net SCL: track 153.7 -> 163.4 mm, vias 8 -> 9
- net Net-(U2-VOUT): track 0.00 -> 6.64 mm
- net +3.3V: track 344.5 -> 339.3 mm
- net Net-(J18-Pin_1): track 8.19 -> 3.46 mm
- net GNDD: track 101.9 -> 106.5 mm
- net Net-(J18-Pin_2): track 0.00 -> 4.21 mm
- net P07: track 35.8 -> 38.5 mm
- net GPIO_INT: track 42.1 -> 39.6 mm
- net Net-(U1-~{RESET}): track 7.27 -> 5.13 mm
- net P10: track 36.6 -> 35.1 mm
- net SDA: track 147.2 -> 148.2 mm
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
